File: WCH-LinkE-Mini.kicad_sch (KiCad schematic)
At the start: 38 parts, among them J2 Conn_02x05_Odd_Even, J3 USB_C_Receptacle_USB2.0_16P, Q1 AO3401A, Q2 AO3401A, Q3 AO3401A, SW1 SW_Push, SW2 SW_Push, U2 CH32V305FBP6, U5 XC6206P332MR-G, Y2 12M

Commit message: fix position
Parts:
- J3: JLCPCB Position Offset 0, 1.02 -> 0, 1
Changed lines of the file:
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@@
 			)
 		)
-		(property "JLCPCB Position Offset" "0, 1.02"
+		(property "JLCPCB Position Offset" "0, 1"
 			(at 48.26 59.69 0)
 			(effects

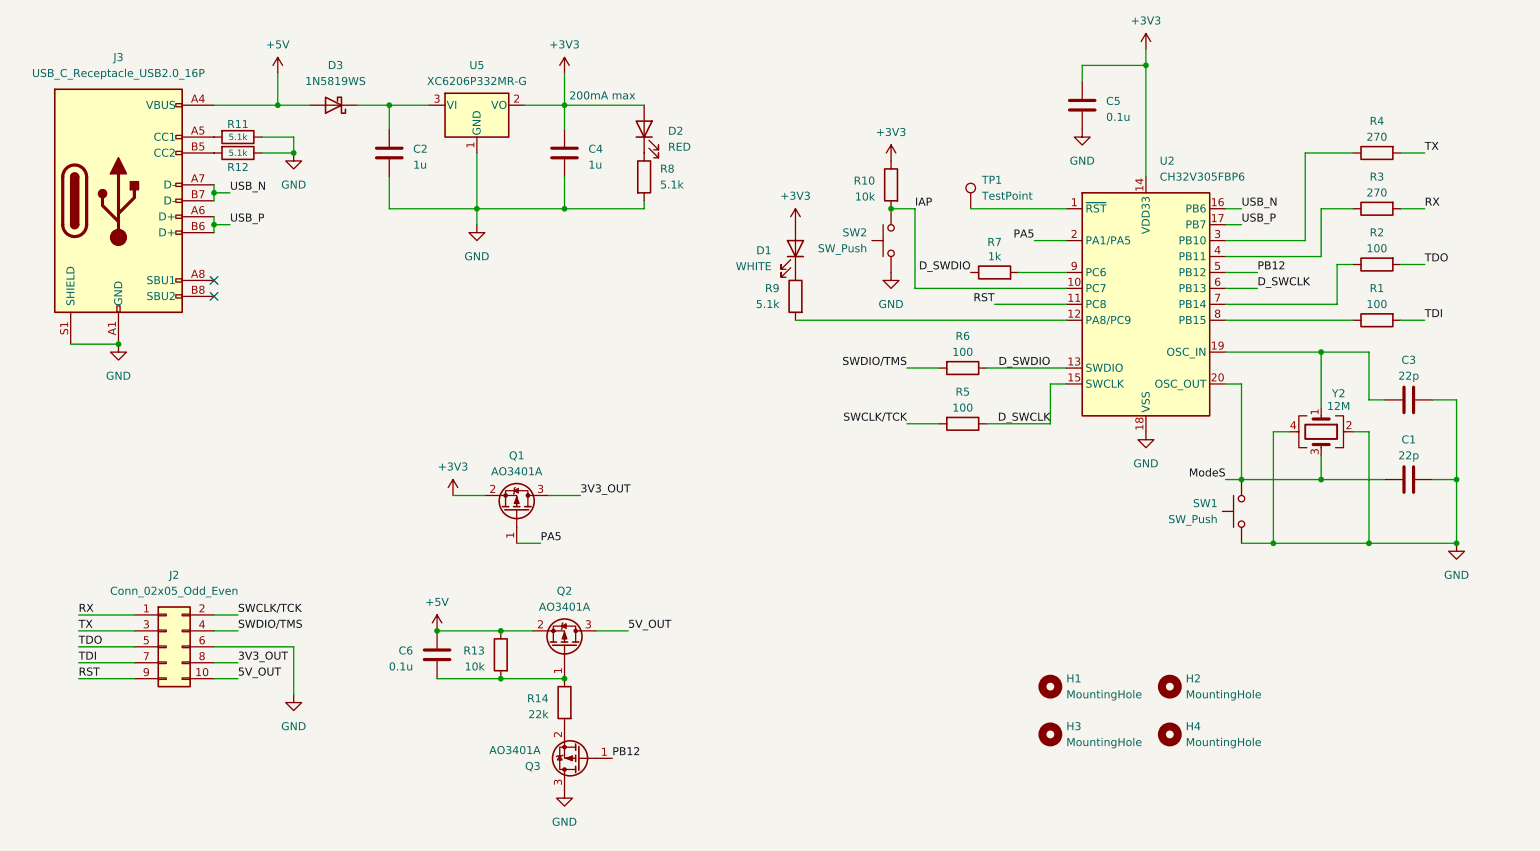
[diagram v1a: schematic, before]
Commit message: change load switch structure
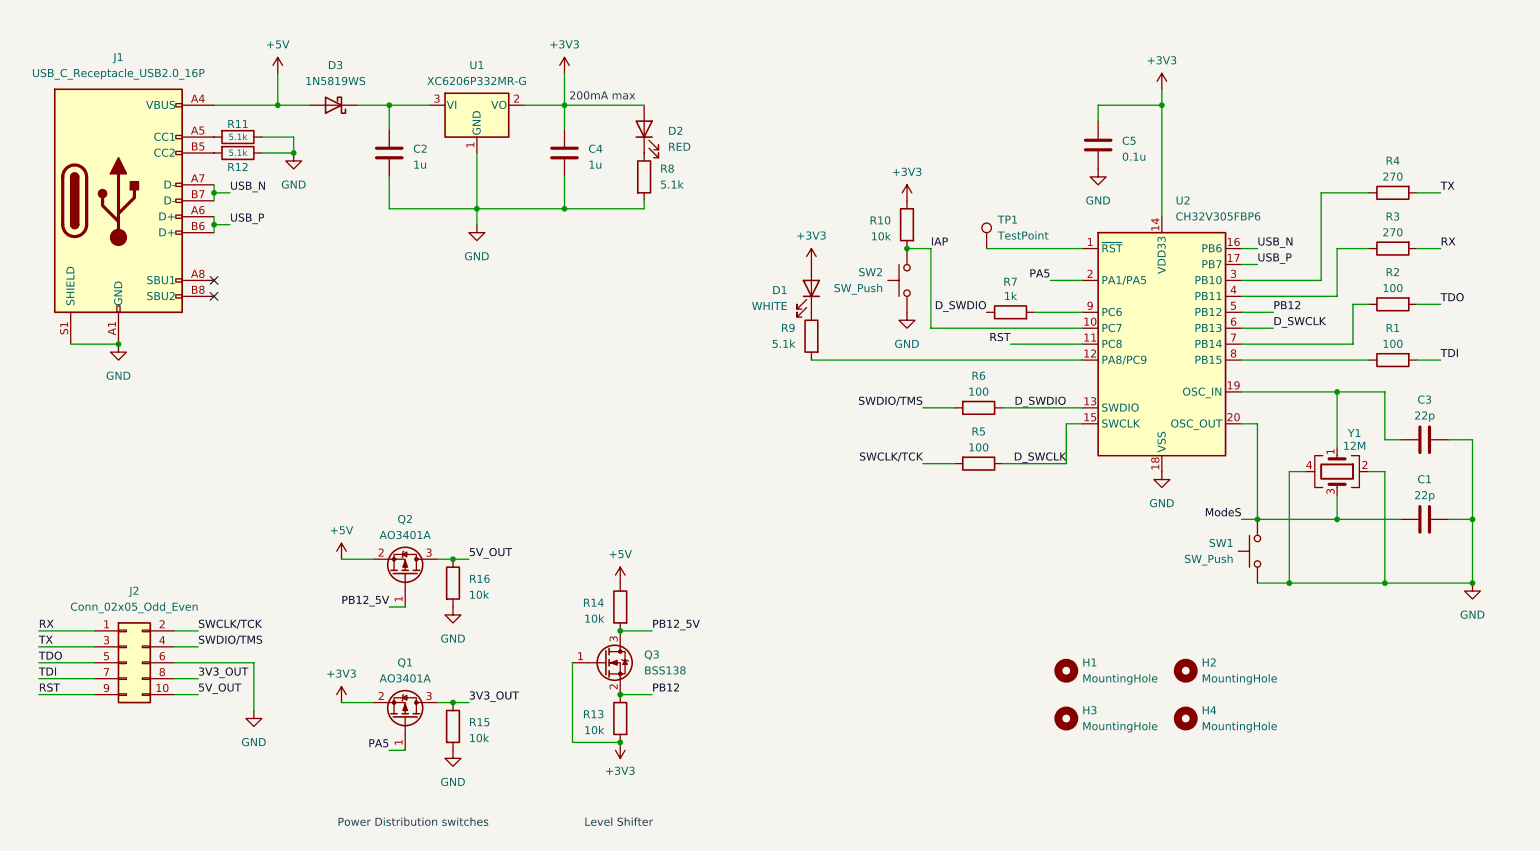
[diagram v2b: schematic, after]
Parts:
- removed C6: 0.1u, Capacitor_SMD:C_0402_1005Metric, symbol Device:C
- removed Q3: AO3401A, Package_TO_SOT_SMD:SOT-23, symbol Transistor_FET:AO3401A
- added Q3: BSS138, Package_TO_SOT_SMD:SOT-23, symbol Transistor_FET:BSS138
- added R15, R16: 10k, Resistor_SMD:R_0402_1005Metric, symbol Device:R
- R14: value 22k -> 10k; LCSC C25768 -> C25744
- renumbered J3 to J1, U5 to U1, Y2 to Y1
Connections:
- net +3V3: now also R13.2, Q3.1 (G)
- net +5V: now also R14.1; no longer R13.1
- net 3V3_OUT: now also R15.1
- net 5V_OUT: now also R16.1
- net GND: now also R15.2, R16.2
- net PB12: now also R13.1, Q3.2 (S)
- net PB12_5V: now reaches R14.2
- net PB12_5V: now also Q2.1 (G), Q3.3 (D)
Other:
- note added: "Level Shifter"
- note added: "Power Distribution switches"
- moved on the sheet: C1, C3, C5, D1, H1, H2, H3, H4, J2, Q1, R1, R10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

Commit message: add remarks
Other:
- note added: "Step down the voltage to increase the current limit of the LDO"
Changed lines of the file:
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@@
+		)
+	)
+	(polyline
+		(pts
+			(xy 82.55 46.99) (xy 82.55 73.66)
+		)
+		(stroke
+			(width 0)
+			(type default)
 		)
 	)
@@
 		(effects
 			(font
+				(size 1.27 1.27)
+			)
+			(justify left)
+		)
+	)
+	(text "Step down the voltage to increase the current limit of the LDO"
+		(exclude_from_sim no)
+		(at 70.866 76.2 0)
+		(effects
+			(font

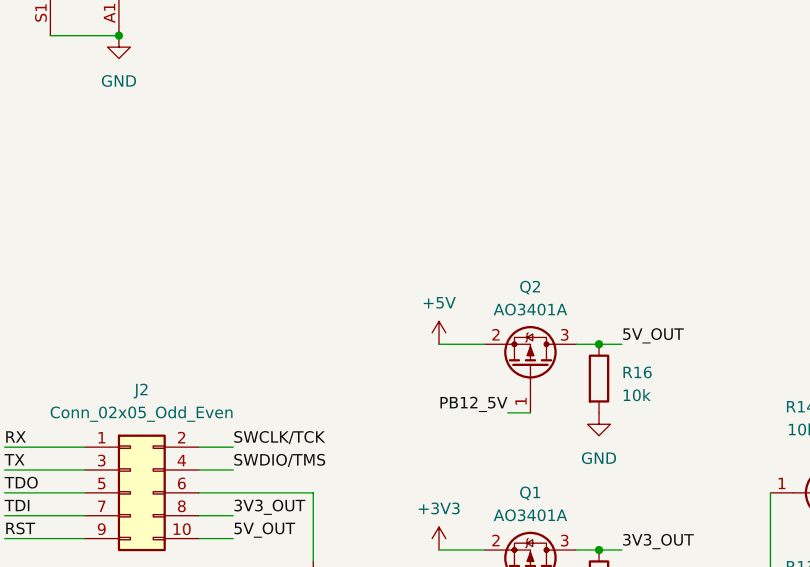
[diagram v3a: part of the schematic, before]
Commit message: add resettable fuse
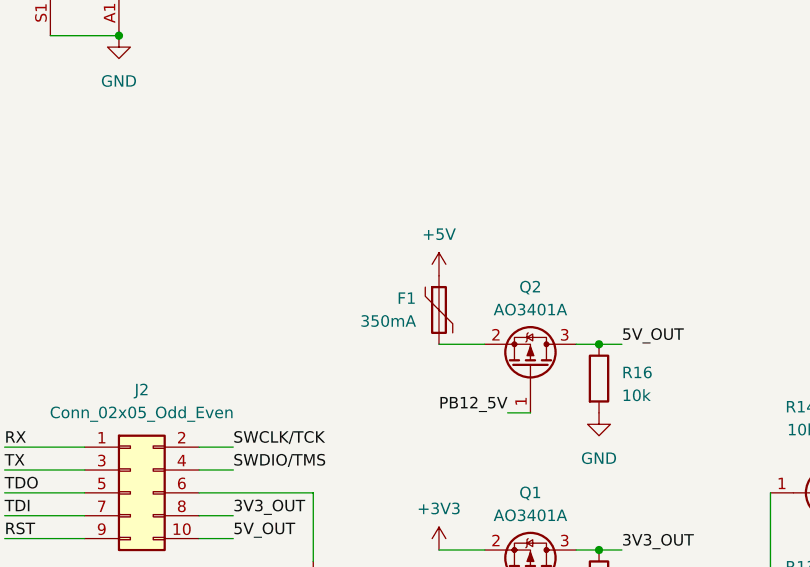
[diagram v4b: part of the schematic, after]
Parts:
- added F1: 350mA, Fuse:Fuse_0603_1608Metric, symbol Device:Polyfuse
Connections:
- net +5V: now also F1.1; no longer Q2.2 (S)
- new net: F1.2, Q2.2 (S)
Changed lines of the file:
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@@
 	(title_block
 		(title "WCH-LinkE-Mini")
-		(rev "v1.1.0")
+		(rev "v1.2.0")
 	)
 	(junction
@@
 	(wire
 		(pts
+			(xy 83.82 116.84) (xy 88.9 116.84)
+		)
+		(stroke
+			(width 0)
+			(type default)
+		)
+	)
+	(wire
+		(pts
 			(xy 196.85 72.39) (xy 201.93 72.39)
 		)
@@
 	(wire
 		(pts
-			(xy 83.82 116.84) (xy 88.9 116.84)
-		)
-		(stroke
-			(width 0)
-			(type default)
-		)
-	)
-	(wire
-		(pts
 			(xy 119.38 44.45) (xy 119.38 48.26)
 		)
@@
 	)
 	(symbol
+		(lib_id "Device:Polyfuse")
+		(at 83.82 113.03 0)
+		(unit 1)
+		(exclude_from_sim no)
+		(in_bom yes)
+		(on_board yes)
+		(dnp no)
+		(property "Reference" "F1"
+			(at 81.28 111.7599 0)
+			(effects
+				(font
+					(size 1.27 1.27)
+				)
+				(justify right)
+			)
+		)
+		(property "Value" "350mA"
+			(at 81.28 114.2999 0)
+			(effects
+				(font
+					(size 1.27 1.27)
+				)
+				(justify right)
+			)
+		)
+		(property "Footprint" "Fuse:Fuse_0603_1608Metric"
+			(at 85.09 118.11 0)
+			(effects
+				(font
+					(size 1.27 1.27)
+				)
+				(justify left)
+				(hide yes)
+			)
+		)
+		(property "Datasheet" "https://wmsc.lcsc.com/wmsc/upload/file/pdf/v2/lcsc/2401210605_LUTE-0603L035-6XR_C7472532.pdf"
+			(at 83.82 113.03 0)
+			(effects
+				(font
+					(size 1.27 1.27)
+				)
+				(hide yes)
+			)
+		)
+		(property "Description" "Resettable fuse, polymeric positive temperature coefficient"
+			(at 83.82 113.03 0)
+			(effects
+				(font
+					(size 1.27 1.27)
+				)
+				(hide yes)
+			)
+		)
+		(property "LCSC" "C7472532"
+			(at 83.82 113.03 0)
+			(effects
+				(font
+					(size 1.27 1.27)
+				)
+				(hide yes)
+			)
+		)
+		(pin "2"
+		)
+		(pin "1"
+		)
+		(instances
+			(project "WCH-LinkE-Mini"
+				(path "/994bdb9a-227d-4e61-bdbf-a26950ab87e1"
+					(reference "F1")
+					(unit 1)
+				)
+			)
+		)
+	)
+	(symbol
 		(lib_id "Device:R")
 		(at 67.31 52.07 270)
@@
 	(symbol
 		(lib_id "power:+5V")
-		(at 83.82 116.84 0)
+		(at 83.82 109.22 0)
 		(unit 1)
 		(exclude_from_sim no)
@@
 		(dnp no)
 		(property "Reference" "#PWR06"
-			(at 83.82 120.65 0)
+			(at 83.82 113.03 0)
 			(effects
 				(font
@@
 		)
 		(property "Value" "+5V"
-			(at 83.82 112.268 0)
+			(at 83.82 104.648 0)
 			(effects
 				(font
@@
 		)
 		(property "Footprint" ""
-			(at 83.82 116.84 0)
+			(at 83.82 109.22 0)
 			(effects
 				(font
@@
 		)
 		(property "Datasheet" ""
-			(at 83.82 116.84 0)
+			(at 83.82 109.22 0)
 			(effects
 				(font
@@
 		)
 		(property "Description" "Power symbol creates a global label with name \"+5V\""
-			(at 83.82 116.84 0)
+			(at 83.82 109.22 0)
 			(effects
 				(font

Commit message: v1.3.0 (#3)
* v1.3.0

* Create review.yml

* remove yml
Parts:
- removed D3: 1N5819WS, Diode_SMD:D_SOD-323, symbol Diode:1N5819WS
- removed F1: 350mA, Fuse:Fuse_0603_1608Metric, symbol Device:Polyfuse
- added D3: B5819WS, Diode_SMD:D_SOD-323, symbol Device:D_Schottky
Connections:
- net +5V: now also C2.1, Q2.2 (S), U1.3 (VI), D3.1 (K); no longer J1.A4 (VBUS), J1.A9 (VBUS), J1.B4 (VBUS), J1.B9 (VBUS)
- new net: D3.2 (A), J1.A4 (VBUS), J1.A9 (VBUS), J1.B4 (VBUS), J1.B9 (VBUS)
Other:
- note removed: "Step down the voltage to increase the current limit of the LDO"

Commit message: v1.3.0
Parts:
- added R17, R18: 10k, Resistor_SMD:R_0402_1005Metric, symbol Device:R
- R15, R16: value 10k -> 330; LCSC C25744 -> C25104
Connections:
- net +3V3: now also R18.1
- net +5V: now also R17.1
- net 3V3_OUT: no longer R15.1
- net 5V_OUT: no longer R16.1
- net GND: no longer R15.2, R16.2
- net PA5: now also R15.2; no longer Q1.1 (G)
- net PB12_5V: now also R16.2; no longer Q2.1 (G)
- new net: Q2.1 (G), R16.1, R17.2
- new net: Q1.1 (G), R15.1, R18.2
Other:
- moved on the sheet: C1, C3, C5, D1, H1, H2, H3, H4, Q1, Q2, Q3, R1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

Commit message: Update to KiCAD 9.0
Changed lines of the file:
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@@
 (kicad_sch
-	(version 20231120)
+	(version 20250114)
 	(generator "eeschema")
-	(generator_version "8.0")
+	(generator_version "9.0")
 	(paper "A4")
 	(title_block
@@
 		(rev "v1.3.0")
 	)
+	(text "Power Distribution switches"
+		(exclude_from_sim no)
+		(at 102.616 160.274 0)
+		(effects
+			(font
+				(size 1.27 1.27)
+			)
+		)
+	)
+	(text "Level Shifter"
+		(exclude_from_sim no)
+		(at 139.446 160.274 0)
+		(effects
+			(font
+				(size 1.27 1.27)
+			)
+		)
+	)
+	(text "200mA max"
+		(exclude_from_sim no)
+		(at 120.142 43.18 0)
+		(effects
+			(font
+				(size 1.27 1.27)
+			)
+			(justify left)
+		)
+	)
 	(junction
 		(at 105.41 60.96)
@@
 		)
 	)
-	(text "Power Distribution switches"
-		(exclude_from_sim no)
-		(at 102.616 160.274 0)
-		(effects
-			(font
-				(size 1.27 1.27)
-			)
-		)
-	)
-	(text "Level Shifter"
-		(exclude_from_sim no)
-		(at 139.446 160.274 0)
-		(effects
-			(font
-				(size 1.27 1.27)
-			)
-		)
-	)
-	(text "200mA max"
-		(exclude_from_sim no)
-		(at 120.142 43.18 0)
-		(effects
-			(font
-				(size 1.27 1.27)
-			)
-			(justify left)
-		)
-	)
 	(label "D_SWDIO"
 		(at 193.04 77.47 180)
-		(fields_autoplaced yes)
 		(effects
 			(font
@@
 	(label "SWDIO{slash}TMS"
 		(at 182.88 92.71 180)
-		(fields_autoplaced yes)
 		(effects
 			(font
@@
 	(label "PB12_5V"
 		(at 144.78 128.27 0)
-		(fields_autoplaced yes)
 		(effects
 			(font
@@
 	(label "RST"
 		(at 35.56 138.43 0)
-		(fields_autoplaced yes)
 		(effects
 			(font
@@
 	(label "SWCLK{slash}TCK"
 		(at 182.88 101.6 180)
-		(fields_autoplaced yes)
 		(effects
 			(font
@@
 	(label "ModeS"
 		(at 233.68 110.49 180)
-		(fields_autoplaced yes)
 		(effects
 			(font
@@
 	(label "USB_N"
 		(at 66.04 58.42 0)
-		(fields_autoplaced yes)
 		(effects
 			(font
@@
 	(label "RST"
 		(at 196.85 82.55 180)
-		(fields_autoplaced yes)
 		(effects
 			(font
@@
 	(label "D_SWDIO"
 		(at 205.74 92.71 180)
-		(fields_autoplaced yes)
 		(effects
 			(font
@@
 	(label "5V_OUT"
 		(at 118.11 116.84 0)
-		(fields_autoplaced yes)
 		(effects
 			(font
@@
 	(label "PA5"
 		(at 87.63 148.59 180)
-		(fields_autoplaced yes)
 		(effects
 			(font
@@
 	(label "TX"
 		(at 265.43 58.42 0)
-		(fields_autoplaced yes)
 		(effects
 			(font
@@
 	(label "PB12"
 		(at 238.76 77.47 0)
-		(fields_autoplaced yes)
 		(effects
 			(font
@@
 	(label "USB_N"
 		(at 236.22 67.31 0)
-		(fields_autoplaced yes)
 		(effects
 			(font
@@
 	(label "TDO"
 		(at 35.56 133.35 0)
-		(fields_autoplaced yes)
 		(effects
 			(font
@@
 	(label "RX"
 		(at 265.43 67.31 0)
-		(fields_autoplaced yes)
 		(effects
 			(font
@@
 	(label "TX"
 		(at 35.56 130.81 0)
-		(fields_autoplaced yes)
 		(effects
 			(font
@@
 	(label "USB_P"
 		(at 236.22 69.85 0)
-		(fields_autoplaced yes)
 		(effects
 			(font
@@
 	(label "RX"
 		(at 35.56 128.27 0)
-		(fields_autoplaced yes)
 		(effects
 			(font
@@
 	(label "3V3_OUT"
 		(at 118.11 140.97 0)
-		(fields_autoplaced yes)
 		(effects
 			(font
@@
 	(label "USB_P"
 		(at 66.04 63.5 0)
-		(fields_autoplaced yes)
 		(effects
 			(font
@@
 	(label "SWCLK{slash}TCK"
 		(at 60.96 128.27 0)
-		(fields_autoplaced yes)
 		(effects
 			(font
@@
 	(label "TDI"
 		(at 265.43 85.09 0)
-		(fields_autoplaced yes)
 		(effects
 			(font
@@
 	(label "D_SWCLK"
 		(at 205.74 101.6 180)
-		(fields_autoplaced yes)
 		(effects
 			(font
@@
 	(label "D_SWCLK"
 		(at 238.76 80.01 0)
-		(fields_autoplaced yes)
 		(effects
 			(font
@@
 	(label "PA5"
 		(at 203.2 72.39 180)
-		(fields_autoplaced yes)
 		(effects
 			(font
@@
 	(label "PB12"
 		(at 144.78 138.43 0)
-		(fields_autoplaced yes)
 		(effects
 			(font
@@
 	(label "PB12_5V"
 		(at 87.63 124.46 180)
-		(fields_autoplaced yes)
 		(effects
 			(font
@@
 	(label "IAP"
 		(at 184.15 67.31 0)
-		(fields_autoplaced yes)
 		(effects
 			(font
@@
 	(label "TDO"
 		(at 265.43 76.2 0)
-		(fields_autoplaced yes)
 		(effects
 			(font
@@
 	(label "TDI"
 		(at 35.56 135.89 0)
-		(fields_autoplaced yes)
 		(effects
 			(font
@@
 	(label "3V3_OUT"
 		(at 60.96 135.89 0)
-		(fields_autoplaced yes)
 		(effects
 			(font
@@
 	(label "SWDIO{slash}TMS"
 		(at 60.96 130.81 0)
-		(fields_autoplaced yes)
 		(effects
 			(font
@@
 	(label "5V_OUT"
 		(at 60.96 138.43 0)
-		(fields_autoplaced yes)
 		(effects
 			(font
@@
 			)
 		)
-		(property "Description" ""
+		(property "Description" "Light emitting diode"
 			(at 132.08 48.26 0)
 			(effects
@@
 			)
 		)
+		(property "Sim.Pins" "1=K 2=A"
+			(at 132.08 48.26 0)
+			(effects
+				(font
+					(size 1.27 1.27)
+				)
+				(hide yes)
+			)
+		)
 		(pin "1"
 		)
@@
 	)
 	(symbol
+		(lib_name "LED_1")
 		(lib_id "Device:LED")
 		(at 165.1 73.66 270)
@@
 			)
 		)
-		(property "Description" ""
+		(property "Description" "Light emitting diode"
 			(at 165.1 73.66 0)
 			(effects
@@
 			)
 		)
+		(property "Sim.Pins" "1=K 2=A"
+			(at 165.1 73.66 0)
+			(effects
+				(font
+					(size 1.27 1.27)
+				)
+				(hide yes)
+			)
+		)
 		(pin "1"
 		)
@@
 		)
 	)
+	(embedded_fonts no)
 )

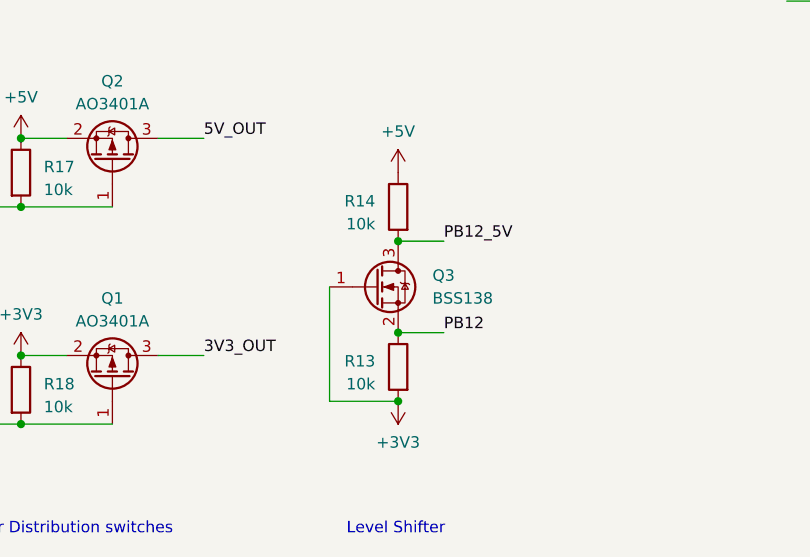
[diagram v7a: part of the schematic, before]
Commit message: update symbols and footprints
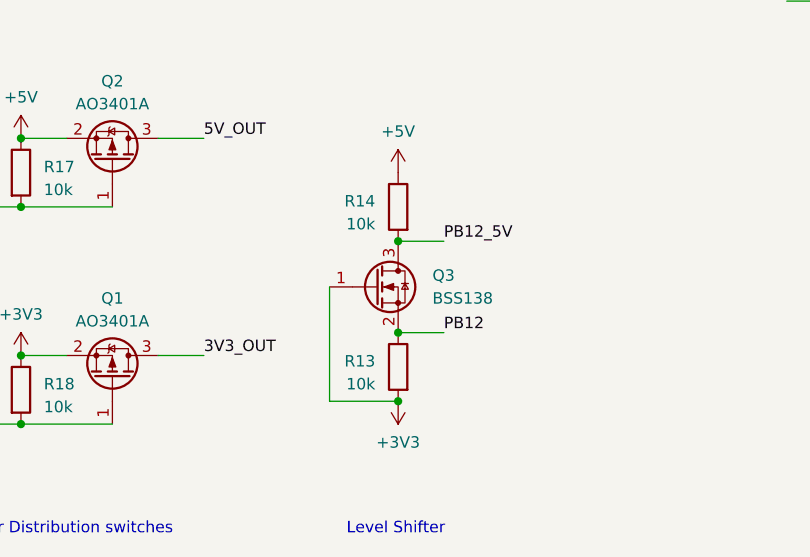
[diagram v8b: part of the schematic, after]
